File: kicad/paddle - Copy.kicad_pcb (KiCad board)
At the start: 4 copper layers, 79.2 x 210.5 mm, 170 parts, among them J1101 CONN_02X05, J301 Battery, M501 MICROSD, P1001 100k, P701 100k, P801 100k, P901 100k, Q201 MMBT4401, Q202 MMBT4401, Q301 DMG3414U, Q302 DMG3415U, Q303 DMG3415U, Q401 DMG3415U, Q501 DMG3415U, SW301 SW_DPDT_x2, U1001 INA333, U1002 ADS1115, U101 BME280, U102 ESP32-WROOM, U1101 SP3003-04, U1102 SP3003-04, U1201 DNP TLVH431, U1202 OPA333, U201 USB_B_Socket, U202 SP3003-04, U203 CP2104, U301 MCP73831/2, U302 NCP694-3.3, U401 FGPMMOPA6H GPS, U601 NCP694-3.3, U701 INA333, U702 ADS1115, U801 INA333, U802 ADS1115, U901 INA333, U902 ADS1115

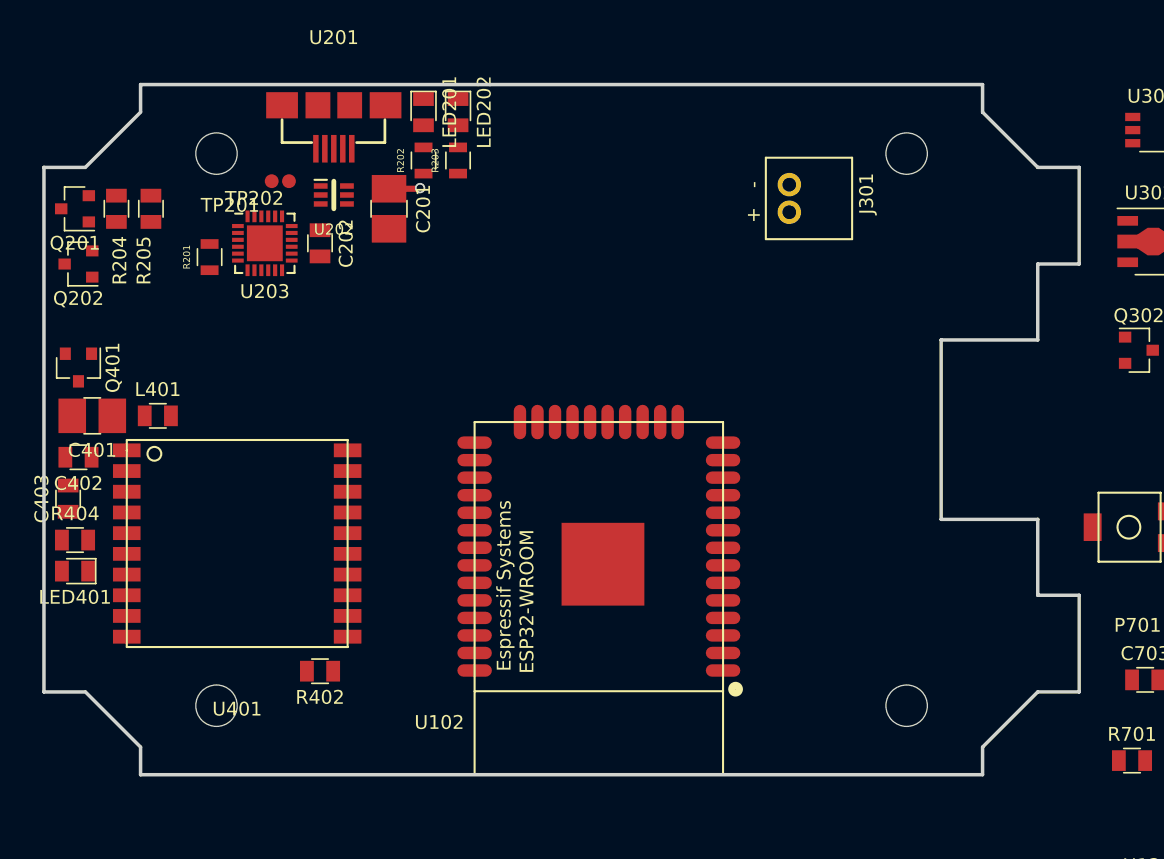
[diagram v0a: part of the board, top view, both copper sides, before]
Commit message: Separate analog block in schematic, fix up board outline, allow for connector, delete bad zones
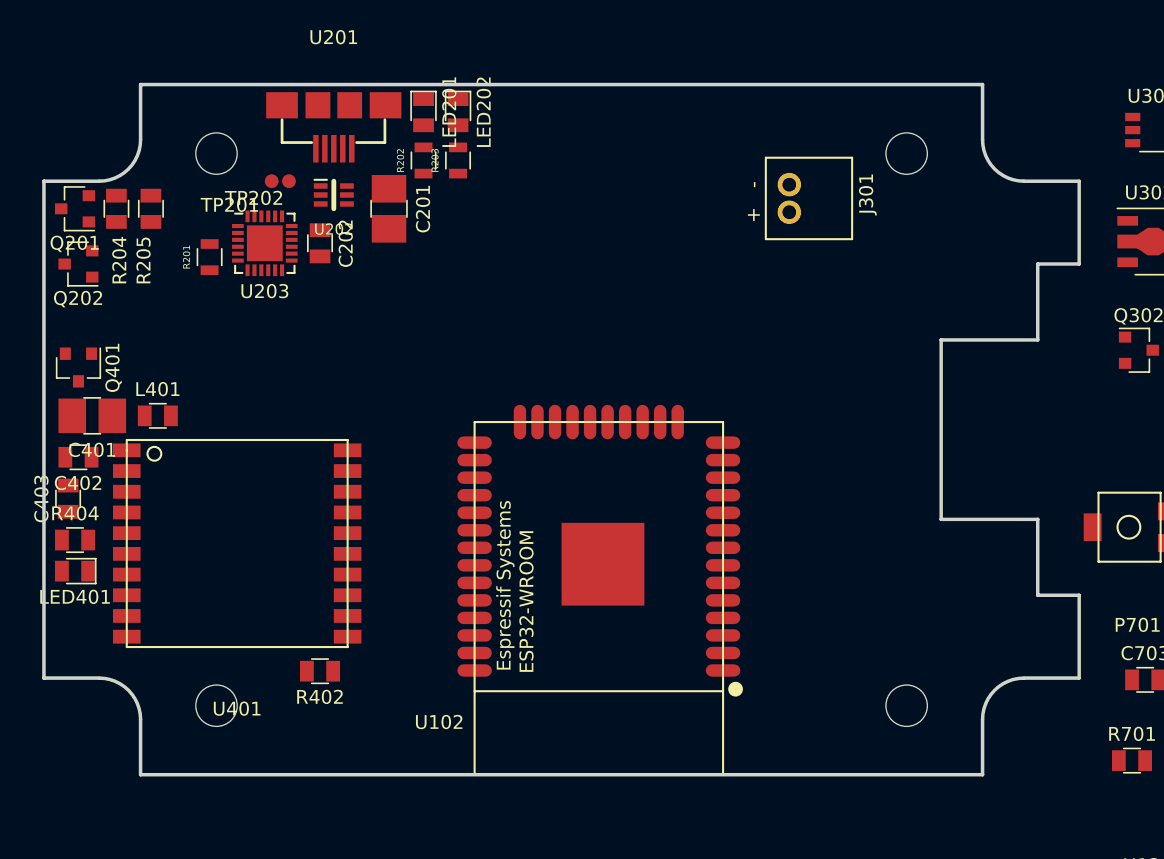
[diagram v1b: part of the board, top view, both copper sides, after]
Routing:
- net +3V3: track 2.27 -> 0.00 mm, vias 1 -> 0
- added copper zone on In1.Cu, net GND
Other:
- outline, holes or cut-outs redrawn
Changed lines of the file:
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@@
     (thickness 1.6)
     (drawings 95)
-    (tracks 3)
+    (tracks 0)
     (zones 0)
     (modules 170)
@@
   )
   (setup
-    (last_trace_width 0.3)
+    (last_trace_width 0.25)
     (user_trace_width 0.3)
     (user_trace_width 0.35)
@@
     )
   )
-  (gr_line (start 118 52) (end 122 56) (angle 90) (layer Edge.Cuts) (width 0.25))
-  (gr_line (start 125 56) (end 122 56) (angle 90) (layer Edge.Cuts) (width 0.25))
-  (gr_line (start 118 50) (end 118 52) (angle 90) (layer Edge.Cuts) (width 0.25))
-  (gr_line (start 118 98) (end 122 94) (angle 90) (layer Edge.Cuts) (width 0.25))
-  (gr_line (start 118 100) (end 118 98) (angle 90) (layer Edge.Cuts) (width 0.25))
-  (gr_line (start 125 94) (end 122 94) (angle 90) (layer Edge.Cuts) (width 0.25))
-  (gr_line (start 53 94) (end 57 98) (angle 90) (layer Edge.Cuts) (width 0.25))
-  (gr_line (start 57 52) (end 53 56) (angle 90) (layer Edge.Cuts) (width 0.25))
   (gr_line (start 118 125) (end 57 125) (layer Edge.Cuts) (width 0.254))
   (gr_line (start 50 132) (end 50 168) (layer Edge.Cuts) (width 0.254))
@@
   (gr_line (start 122 81.5) (end 122 87) (angle 90) (layer Edge.Cuts) (width 0.25))
   (gr_line (start 122 63) (end 122 68.5) (angle 90) (layer Edge.Cuts) (width 0.25))
-  (gr_line (start 125 94) (end 125 87) (angle 90) (layer Edge.Cuts) (width 0.25))
-  (gr_line (start 125 56) (end 125 63) (angle 90) (layer Edge.Cuts) (width 0.25))
+  (gr_line (start 125 93) (end 125 87) (angle 90) (layer Edge.Cuts) (width 0.25))
+  (gr_line (start 125 57) (end 125 63) (angle 90) (layer Edge.Cuts) (width 0.25))
   (gr_line (start 115 81.5) (end 122 81.5) (angle 90) (layer Edge.Cuts) (width 0.25))
   (gr_line (start 115 68.5) (end 115 81.5) (angle 90) (layer Edge.Cuts) (width 0.25))
@@
   (target plus (at 125 50) (size 5) (width 0.15) (layer Edge.Cuts))
   (target plus (at 50 100) (size 5) (width 0.15) (layer Edge.Cuts))
-  (gr_line (start 50 56) (end 53 56) (layer Edge.Cuts) (width 0.254))
-  (gr_line (start 57 52) (end 57 50) (layer Edge.Cuts) (width 0.254))
-  (gr_line (start 57 98) (end 57 100) (layer Edge.Cuts) (width 0.254))
-  (gr_line (start 50 94) (end 53 94) (layer Edge.Cuts) (width 0.254))
+  (gr_line (start 50 57) (end 54 57) (layer Edge.Cuts) (width 0.254))
+  (gr_arc (start 54 54) (end 57 54) (angle 90) (layer Edge.Cuts) (width 0.25))
+  (gr_line (start 57 54) (end 57 50) (layer Edge.Cuts) (width 0.254))
+  (gr_arc (start 54 96) (end 57 96) (angle -90) (layer Edge.Cuts) (width 0.25))
+  (gr_line (start 57 96) (end 57 100) (layer Edge.Cuts) (width 0.254))
+  (gr_line (start 50 93) (end 54 93) (layer Edge.Cuts) (width 0.254))
+  (gr_line (start 121 93) (end 125 93) (layer Edge.Cuts) (width 0.254))
+  (gr_line (start 118 100) (end 118 96) (layer Edge.Cuts) (width 0.254))
+  (gr_arc (start 121 96) (end 121 93) (angle -90) (layer Edge.Cuts) (width 0.25))
+  (gr_arc (start 121 54) (end 121 57) (angle 90) (layer Edge.Cuts) (width 0.25))
   (gr_line (start 57 100) (end 118 100) (layer Edge.Cuts) (width 0.254))
-  (gr_line (start 50 56) (end 50 94) (layer Edge.Cuts) (width 0.254))
+  (gr_line (start 121 57) (end 125 57) (layer Edge.Cuts) (width 0.254))
+  (gr_line (start 118 50) (end 118 54) (layer Edge.Cuts) (width 0.254))
+  (gr_line (start 50 57) (end 50 93) (layer Edge.Cuts) (width 0.254))
   (gr_line (start 118 50) (end 57 50) (layer Edge.Cuts) (width 0.254))
-  (segment (start 75 57.55) (end 77.2 57.55) (width 0.45) (layer F.Cu) (net 1))
-  (via (at 77.25 57.5) (size 0.75) (drill 0.5) (layers F.Cu B.Cu) (net 1))
-  (segment (start 77.2 57.55) (end 77.25 57.5) (width 0.45) (layer F.Cu) (net 1))
-  (zone (net 2) (net_name GND) (layer In2.Cu) (hatch edge 0.508)
+  (zone (net 2) (net_name GND) (layer In1.Cu) (hatch edge 0.508)
     (connect_pads (clearance 0.2))
     (min_thickness 0.2)
@@
     (polygon
       (pts
-        (xy 50 50) (xy 125 50) (xy 125 100) (xy 50 100)
+        (xy -153 -18) (xy -78 -18) (xy -78 32) (xy -153 32)
       )
     )
@@
     (polygon
       (pts
-        (xy 50 50) (xy 125 50) (xy 125 100) (xy 50 100)
+        (xy -153 -18) (xy -78 -18) (xy -78 32) (xy -153 32)
+      )
+    )
+  )
+  (zone (net 2) (net_name GND) (layer In2.Cu) (hatch edge 0.508)
+    (connect_pads (clearance 0.2))
+    (min_thickness 0.2)
+    (fill yes (arc_segments 16) (thermal_gap 0.508) (thermal_bridge_width 0.508))
+    (polygon
+      (pts
+        (xy -153 -18) (xy -78 -18) (xy -78 32) (xy -153 32)
+      )
+    )
+  )
+  (zone (net 2) (net_name GND) (layer In2.Cu) (hatch edge 0.508)
+    (connect_pads (clearance 0.2))
+    (min_thickness 0.2)
+    (fill yes (arc_segments 16) (thermal_gap 0.508) (thermal_bridge_width 0.508))
+    (polygon
+      (pts
+        (xy -153 57) (xy -78 57) (xy -78 107) (xy -153 107)
       )
     )
